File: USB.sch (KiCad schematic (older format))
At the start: 21 parts, among them IC3 USBLC6-4, IC5 USB3300, P1 MICROUSBAB, Q1 BC850

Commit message: #3 Add SD card interface #4 Add CAN & UART transceivers
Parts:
- removed C18: 4u7, ~, symbol CP1
- added C1: 4u7, symbol C
- added D2: D, symbol D
- C10: renamed from C15; symbol C -> C-RESCUE-Noodleboard
- C2: renamed from C19; symbol C -> C-RESCUE-Noodleboard
- C3: renamed from C20; symbol C -> C-RESCUE-Noodleboard
- C4: renamed from C21; symbol CP1 -> CP1-RESCUE-Noodleboard
- C5: renamed from C22; symbol CP1 -> CP1-RESCUE-Noodleboard
- C6: renamed from C26; symbol C -> C-RESCUE-Noodleboard
- C7: renamed from C27; symbol C -> C-RESCUE-Noodleboard
- C8: renamed from C33; symbol C -> C-RESCUE-Noodleboard
- C9: renamed from C23; symbol C -> C-RESCUE-Noodleboard
- D1: renamed from D6; symbol LED -> LED-RESCUE-Noodleboard
- IC2: renamed from IC5; symbol USB3300 -> USB3300-RESCUE-Noodleboard
- R1: renamed from R11; symbol R -> R-RESCUE-Noodleboard
- R2: renamed from R12; symbol R -> R-RESCUE-Noodleboard
- R3: renamed from R13; symbol R -> R-RESCUE-Noodleboard
- R4: renamed from R19; symbol R -> R-RESCUE-Noodleboard
- R5: renamed from R20; symbol R -> R-RESCUE-Noodleboard
- renumbered IC3 to IC1
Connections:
- net labels added: 3V3_L, CLK_L, D0_L, D1_L, D2_L, D3_L, D4_L, D5_L, D6_L, D7_L, DIR_L, GND_L, NXT_L, STP_L, USB_D+, USB_D-, VUSB_5V0, VUSB_5V0_L
- net labels removed: 3V3_USB, 5V0, 5V_USB, GND_USB, VBUS_HS_0
- wire segments 73 -> 97
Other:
- note added: "Connector\n"
- note added: "ESD protection\n"
- note added: "Power signaling\n"
- note added: "Power supply\n"
- note added: "USB MCU Interface\n"
- note added: "USB ULPI\n"
- note removed: "Hierarchical Pins\n(External)\n"
- moved on the sheet: C10, C2, C3, C6, C7, C8, C9, IC1, OSC1, P1, Q1, R1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

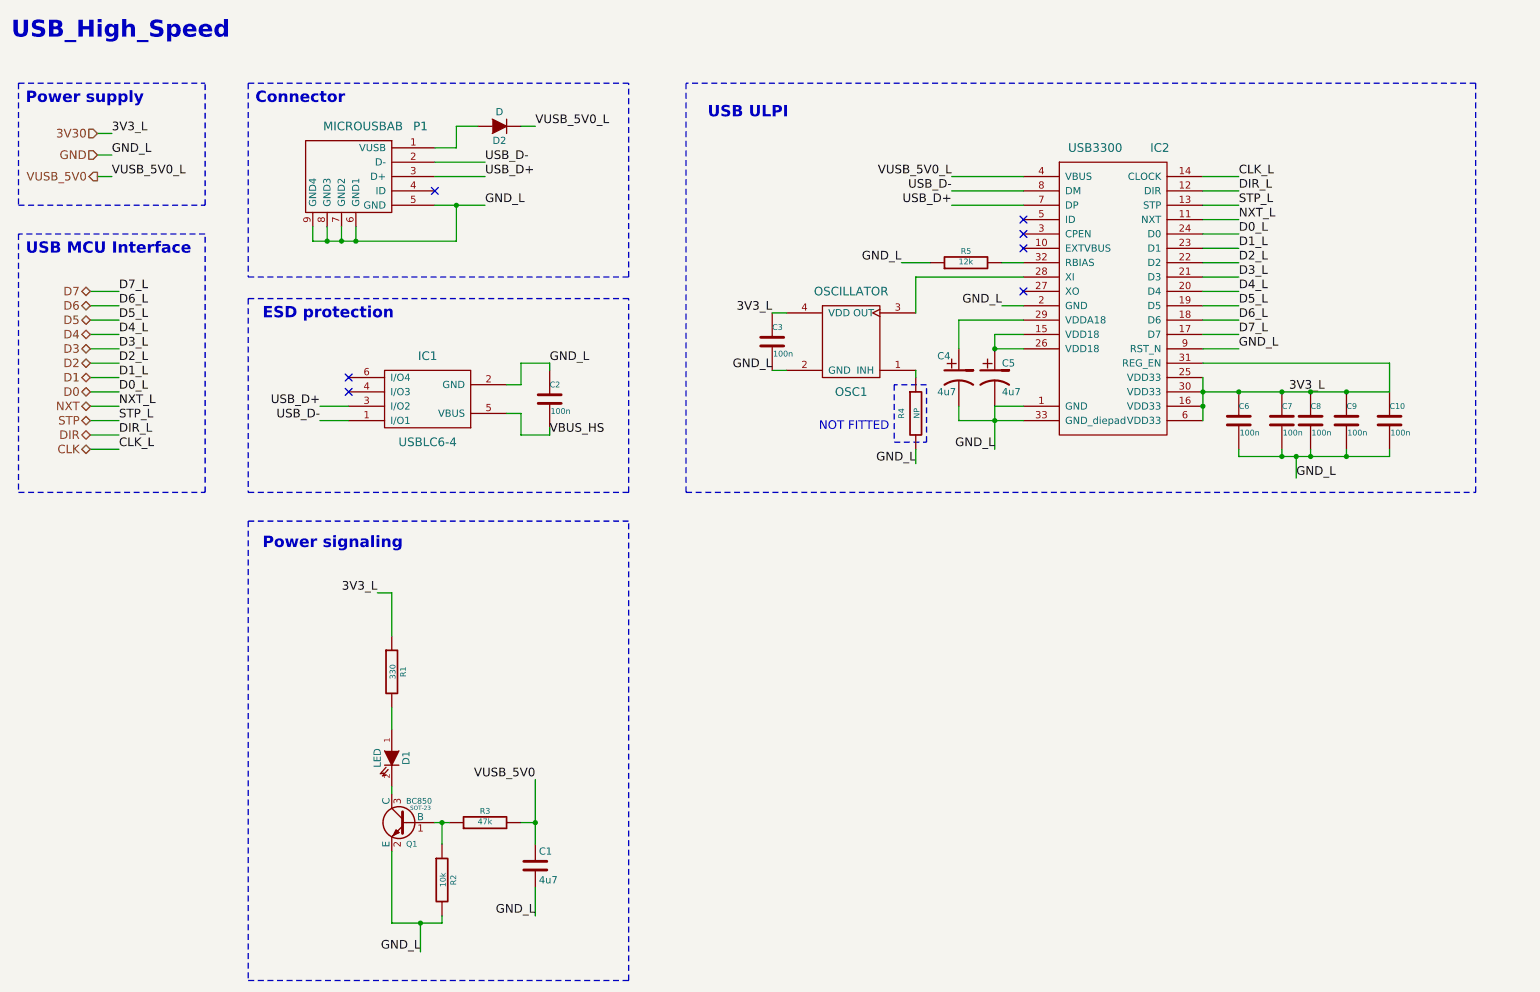
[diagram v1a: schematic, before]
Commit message: - #4 Added UART and CAN interface transceivers - Improved schematic structure - Removed all gerber outputs - Generated schematics outputs for PCB design - Updated local libraries
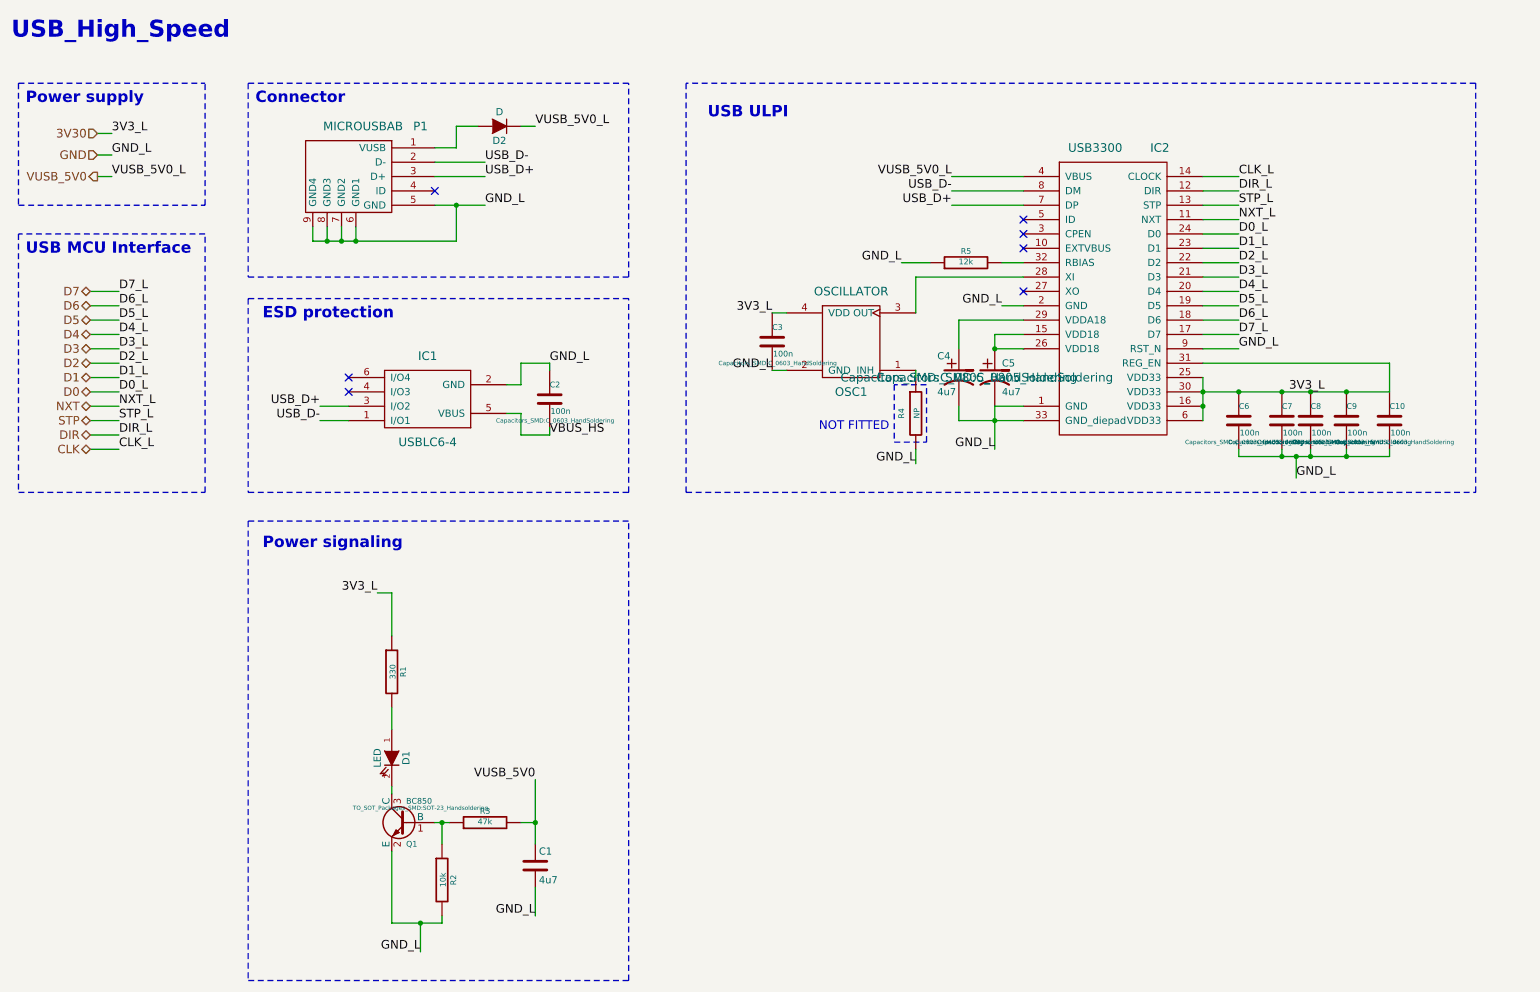
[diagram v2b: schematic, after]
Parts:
- C1: footprint (none) -> Capacitors_SMD:C_0805_HandSoldering
- C10, C2, C3, C6, C7, C8, C9: footprint ~ -> Capacitors_SMD:C_0603_HandSoldering
- C4, C5: footprint ~ -> Capacitors_SMD:C_0805_HandSoldering
- D1: footprint ~ -> LEDs:LED-0805
- D2: footprint (none) -> Diodes_SMD:SMA_Handsoldering
- IC1: footprint (none) -> TO_SOT_Packages_SMD:SOT-23-6
- IC2: footprint ~ -> Housings_DFN_QFN:QFN-32-1EP_5x5mm_Pitch0.5mm
- OSC1: footprint (none) -> ComponentLib:26MHZOSC
- P1: footprint (none) -> ComponentLibv2:uUSB-AB
- Q1: footprint SOT-23 -> TO_SOT_Packages_SMD:SOT-23_Handsoldering
- R1, R2, R3, R4, R5: footprint ~ -> Resistors_SMD:R_0603_HandSoldering
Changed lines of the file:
@@
 F 0 "P1" H 3450 2050 60  0000 C CNN
 F 1 "MICROUSBAB" H 3050 2050 60  0000 C CNN
-F 2 "" H 3050 1700 60  0000 C CNN
-F 3 "" H 3050 1700 60  0000 C CNN
+F 2 "ComponentLibv2:uUSB-AB" H 3050 1700 60  0001 C CNN
+F 3 "http://www.farnell.com/datasheets/44939.pdf" H 3050 1700 60  0001 C CNN
 	1    3050 1700
 	1    0    0    -1
@@
 F 0 "IC1" H 3500 2950 60  0000 C CNN
 F 1 "USBLC6-4" H 3500 3550 60  0000 C CNN
-F 2 "" H 3500 3250 60  0000 C CNN
+F 2 "TO_SOT_Packages_SMD:SOT-23-6" H 3500 3250 60  0001 C CNN
 F 3 "" H 3500 3250 60  0000 C CNN
 	1    3500 3250
@@
 F 0 "C2" H 4350 3350 40  0000 L CNN
 F 1 "100n" H 4356 3165 40  0000 L CNN
-F 2 "~" H 4388 3100 30  0000 C CNN
+F 2 "Capacitors_SMD:C_0603_HandSoldering" H 4388 3100 30  0000 C CNN
 F 3 "~" H 4350 3250 60  0000 C CNN
 	1    4350 3250
@@
 F 0 "R1" V 3330 5150 40  0000 C CNN
 F 1 "330" V 3257 5151 40  0000 C CNN
-F 2 "~" V 3180 5150 30  0000 C CNN
+F 2 "Resistors_SMD:R_0603_HandSoldering" V 3180 5150 30  0001 C CNN
 F 3 "~" H 3250 5150 30  0000 C CNN
 	1    3250 5150
@@
 F 0 "D1" H 3250 5850 50  0000 C CNN
 F 1 "LED" H 3250 5650 50  0000 C CNN
-F 2 "~" H 3250 5750 60  0000 C CNN
+F 2 "LEDs:LED-0805" H 3250 5750 60  0001 C CNN
 F 3 "~" H 3250 5750 60  0000 C CNN
 	1    3250 5750
@@
 F 0 "Q1" H 3350 6051 40  0000 R CNN
 F 1 "BC850" H 3350 6350 40  0000 R CNN
-F 2 "SOT-23" H 3250 6302 29  0000 C CNN
+F 2 "TO_SOT_Packages_SMD:SOT-23_Handsoldering" H 3250 6302 29  0000 C CNN
 F 3 "" H 3350 6200 60  0000 C CNN
 	1    3350 6200
@@
 F 0 "R2" V 3680 6600 40  0000 C CNN
 F 1 "10k" V 3607 6601 40  0000 C CNN
-F 2 "~" V 3530 6600 30  0000 C CNN
+F 2 "Resistors_SMD:R_0603_HandSoldering" V 3530 6600 30  0001 C CNN
 F 3 "~" H 3600 6600 30  0000 C CNN
 	1    3600 6600
@@
 F 0 "R3" V 3980 6200 40  0000 C CNN
 F 1 "47k" V 3907 6201 40  0000 C CNN
-F 2 "~" V 3830 6200 30  0000 C CNN
+F 2 "Resistors_SMD:R_0603_HandSoldering" V 3830 6200 30  0001 C CNN
 F 3 "~" H 3900 6200 30  0000 C CNN
 	1    3900 6200
@@
 F 0 "R5" V 7330 2300 40  0000 C CNN
 F 1 "12k" V 7257 2301 40  0000 C CNN
-F 2 "~" V 7180 2300 30  0000 C CNN
+F 2 "Resistors_SMD:R_0603_HandSoldering" V 7180 2300 30  0001 C CNN
 F 3 "~" H 7250 2300 30  0000 C CNN
 F 4 "1%" V 7250 2300 60  0001 C CNN "Tolerancia"
@@
 F 0 "OSC1" H 6450 2600 60  0000 C CNN
 F 1 "OSCILLATOR" H 6450 3300 60  0000 C CNN
-F 2 "" H 6450 2900 60  0000 C CNN
+F 2 "ComponentLib:26MHZOSC" H 6450 2900 60  0001 C CNN
 F 3 "" H 6450 2900 60  0000 C CNN
 	1    6450 2900
@@
 F 0 "C3" H 5900 2950 40  0000 L CNN
 F 1 "100n" H 5906 2765 40  0000 L CNN
-F 2 "~" H 5938 2700 30  0000 C CNN
+F 2 "Capacitors_SMD:C_0603_HandSoldering" H 5938 2700 30  0000 C CNN
 F 3 "~" H 5900 2850 60  0000 C CNN
 	1    5900 2850
@@
 F 0 "R4" V 6800 3350 40  0000 C CNN
 F 1 "NP" V 6907 3351 40  0000 C CNN
-F 2 "~" V 6830 3350 30  0000 C CNN
+F 2 "Resistors_SMD:R_0603_HandSoldering" V 6830 3350 30  0001 C CNN
 F 3 "~" H 6900 3350 30  0000 C CNN
 	1    6900 3350
@@
 F 0 "C7" H 9450 3500 40  0000 L CNN
 F 1 "100n" H 9456 3315 40  0000 L CNN
-F 2 "~" H 9488 3250 30  0000 C CNN
+F 2 "Capacitors_SMD:C_0603_HandSoldering" H 9488 3250 30  0000 C CNN
 F 3 "~" H 9450 3400 60  0000 C CNN
 	1    9450 3400
@@
 F 0 "C6" H 9150 3500 40  0000 L CNN
 F 1 "100n" H 9156 3315 40  0000 L CNN
-F 2 "~" H 9188 3250 30  0000 C CNN
+F 2 "Capacitors_SMD:C_0603_HandSoldering" H 9188 3250 30  0000 C CNN
 F 3 "~" H 9150 3400 60  0000 C CNN
 	1    9150 3400
@@
 F 0 "C8" H 9650 3500 40  0000 L CNN
 F 1 "100n" H 9656 3315 40  0000 L CNN
-F 2 "~" H 9688 3250 30  0000 C CNN
+F 2 "Capacitors_SMD:C_0603_HandSoldering" H 9688 3250 30  0000 C CNN
 F 3 "~" H 9650 3400 60  0000 C CNN
 	1    9650 3400
@@
 F 0 "C4" H 7050 3250 50  0000 L CNN
 F 1 "4u7" H 7050 3000 50  0000 L CNN
-F 2 "~" H 7200 3100 60  0000 C CNN
+F 2 "Capacitors_SMD:C_0805_HandSoldering" H 7200 3100 60  0000 C CNN
 F 3 "~" H 7200 3100 60  0000 C CNN
 	1    7200 3100
@@
 F 0 "C5" H 7500 3200 50  0000 L CNN
 F 1 "4u7" H 7500 3000 50  0000 L CNN
-F 2 "~" H 7450 3100 60  0000 C CNN
+F 2 "Capacitors_SMD:C_0805_HandSoldering" H 7450 3100 60  0000 C CNN
 F 3 "~" H 7450 3100 60  0000 C CNN
 	1    7450 3100
@@
 F 0 "C9" H 9900 3500 40  0000 L CNN
 F 1 "100n" H 9906 3315 40  0000 L CNN
-F 2 "~" H 9938 3250 30  0000 C CNN
+F 2 "Capacitors_SMD:C_0603_HandSoldering" H 9938 3250 30  0000 C CNN
 F 3 "~" H 9900 3400 60  0000 C CNN
 	1    9900 3400
@@
 F 0 "IC2" H 8600 2900 60  0000 C CNN
 F 1 "USB3300" H 8150 2900 60  0000 C CNN
-F 2 "~" H 8300 2200 60  0000 C CNN
+F 2 "Housings_DFN_QFN:QFN-32-1EP_5x5mm_Pitch0.5mm" H 8300 2200 60  0001 C CNN
 F 3 "~" H 8300 2200 60  0000 C CNN
 	1    8300 2200
@@
 F 0 "C10" H 10200 3500 40  0000 L CNN
 F 1 "100n" H 10206 3315 40  0000 L CNN
-F 2 "~" H 10238 3250 30  0000 C CNN
+F 2 "Capacitors_SMD:C_0603_HandSoldering" H 10238 3250 30  0000 C CNN
 F 3 "~" H 10200 3400 60  0000 C CNN
 	1    10200 3400
@@
 F 0 "C1" H 4275 6600 50  0000 L CNN
 F 1 "4u7" H 4275 6400 50  0000 L CNN
-F 2 "" H 4288 6350 30  0000 C CNN
+F 2 "Capacitors_SMD:C_0805_HandSoldering" H 4288 6350 30  0001 C CNN
 F 3 "" H 4250 6500 60  0000 C CNN
 	1    4250 6500
@@
 F 0 "D2" H 4000 1450 50  0000 C CNN
 F 1 "D" H 4000 1250 50  0000 C CNN
-F 2 "" H 4000 1350 60  0000 C CNN
+F 2 "Diodes_SMD:SMA_Handsoldering" H 4000 1350 60  0001 C CNN
 F 3 "" H 4000 1350 60  0000 C CNN
 	1    4000 1350

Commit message: #5 Review USB power supply #6 Power signaling LED should be in power sheet - Simplified outputs (Gerber, sch & pcb)
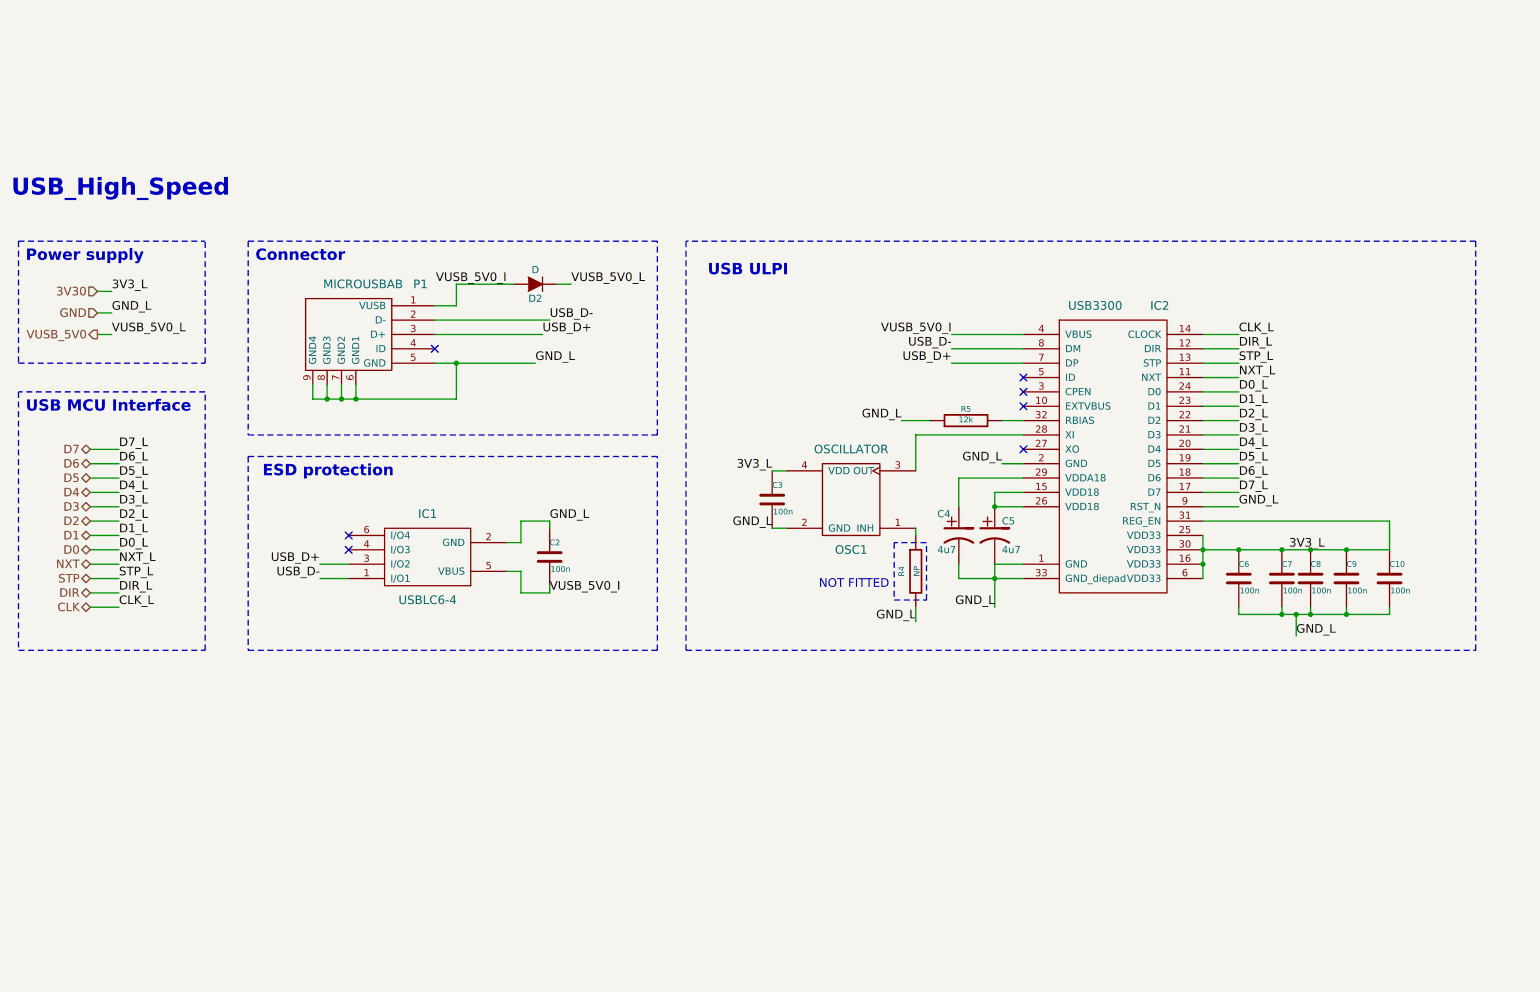
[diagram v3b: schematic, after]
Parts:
- removed C1: 4u7, Capacitors_SMD:C_0805_HandSoldering, symbol C
- removed D1: LED, LEDs:LED-0805, symbol LED-RESCUE-Noodleboard
- removed Q1: BC850, TO_SOT_Packages_SMD:SOT-23_Handsoldering, symbol BC850
- removed R1: 330, Resistors_SMD:R_0603_HandSoldering, symbol R-RESCUE-Noodleboard
- removed R2: 10k, Resistors_SMD:R_0603_HandSoldering, symbol R-RESCUE-Noodleboard
- removed R3: 47k, Resistors_SMD:R_0603_HandSoldering, symbol R-RESCUE-Noodleboard
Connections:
- net VBUS_HS is gone; now on net VUSB_5V0_I: C2.2, IC1.5 (VBUS)
- net VUSB_5V0: no longer IC2.4 (VBUS)
- net VUSB_5V0_I: now reaches D2.2 (A), P1.1 (VUSB)
- net VUSB_5V0_I: now also IC2.4 (VBUS)
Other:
- note removed: "Power signaling\n"
- moved on the sheet: C10, C2, C3, C4, C5, C6, C7, C8, C9, D2, IC1, IC2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
